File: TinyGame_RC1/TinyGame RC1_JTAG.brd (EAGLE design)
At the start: 38 x 22 mm, 41 parts, among them J1 AUDIO-CONNECTOR-6P-SMD-344003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, K1 BUTTON-4P-3100010P1, K2 BUTTON-4P-3100010P1, K3 BUTTON-4P-3100010P1, K4 BUTTON-4P-3100010P1, U1 MKL02Z32VFK4

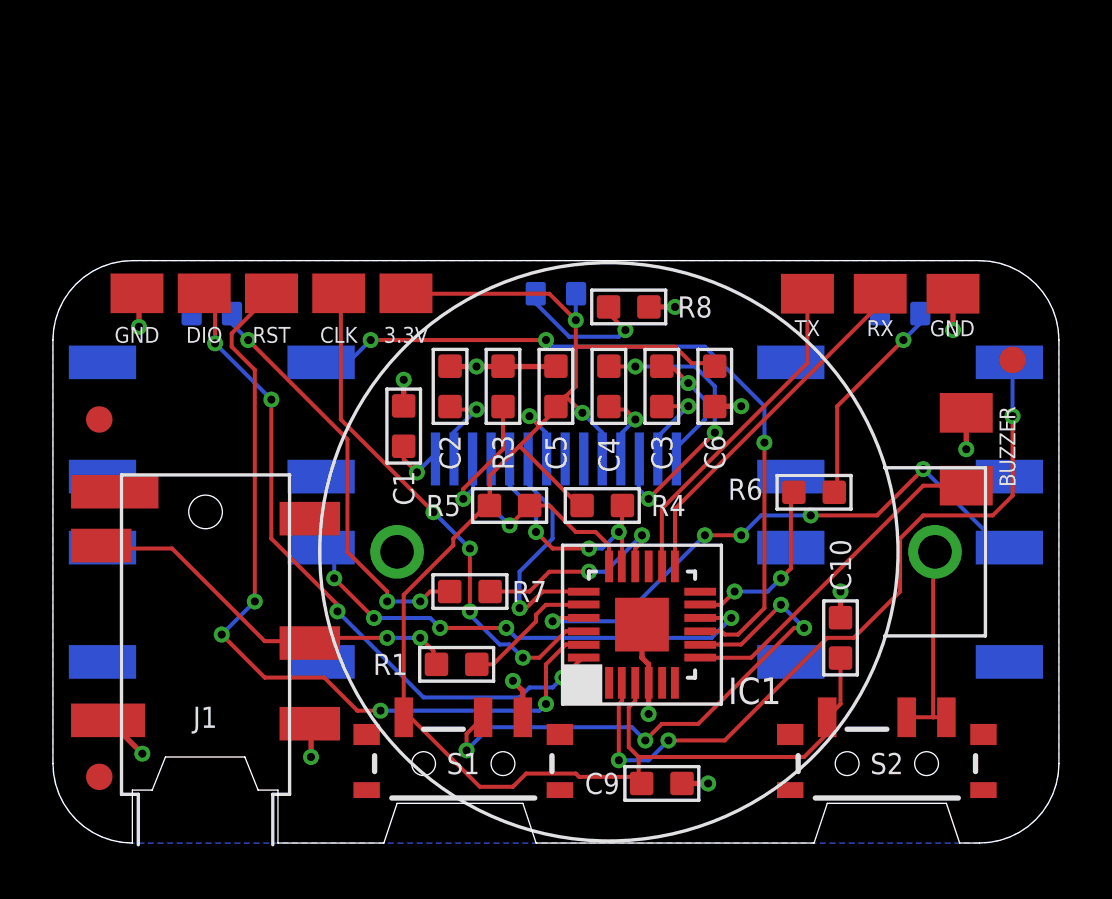
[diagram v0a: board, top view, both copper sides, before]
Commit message: Moved some stuff around - added testjig and jtag adapter
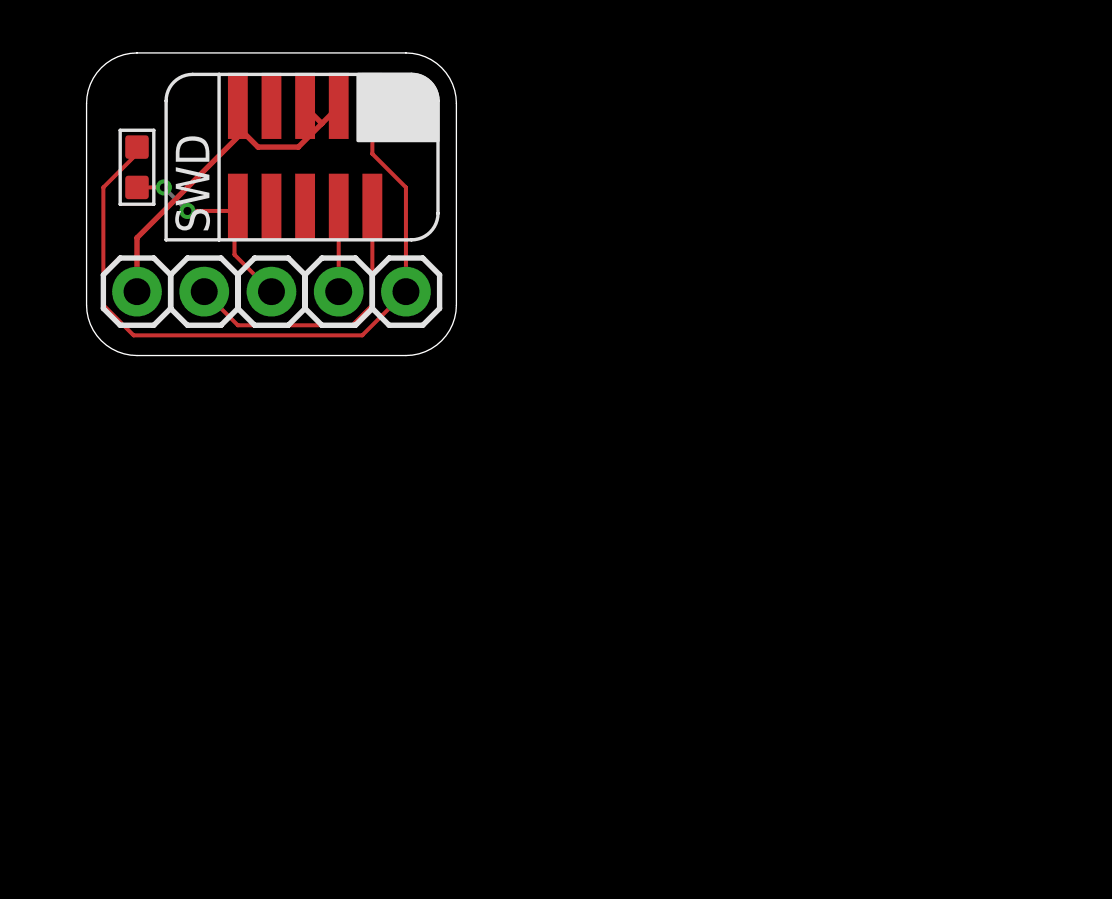
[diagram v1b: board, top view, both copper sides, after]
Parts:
- removed AUDIOGND, AUDIOSIG, PTA6_MISO1, PTA6_MISO2, PTA6_MISO3, PTA6_MISO4, PTA6_MISO5, PTB1_RXTX, PTB2_TXRX, PTB2_TXRX2: M01SMD-4.5X1.5, SparkFun-Connectors:PAD-1.5X4.5
- removed BATTERY_1: BATTERY_1236_C, MicroGameboyParts:BATTERY_1236_C
- removed C1: 2.2uF, OPL:C0603
- removed C10: 100nF, OPL:C0603
- removed C2: 4.7uF, OPL:C0603
- removed C3, C4, C5, C6, C9: 1uF, OPL:C0603
- removed D1, D2, D3: YELLOW, OPL:LED0603
- removed J1: AUDIO-CONNECTOR-6P-SMD-3440030P1, OPL:6P-SMD-3.5
- removed K1, K2, K3, K4: BUTTON-4P-3100010P1, zephod-components:4P-SMD-6.0X6.0X5.0H
- removed R1, R4, R5, R6, R7: 2K, OPL:R0603
- removed R3: 390K, OPL:R0603
- removed S1, S2: (no value), SparkFun-Electromechanical:SWITCH-SPST-SMD-A
- removed U$1: 0.49"OLEDFOLDED, zephod-tft:0.49"-FPC-0.7-14-FOLDED
- removed U$2, U$3, U$4: FIDUCIAL, adafruit:FIDUCIAL_1MM
- removed U1: MKL02Z32VFK4, FarnellThings:QFN50P400X400X100-25N
- added 3.3V_1, GND_2, RESET, SWCLK, SWDIO: M01PTH, SparkFun-Connectors:1X01
- added SWD1: CORTEX_SWDVERT, carrilib with jtags:SWD_VERTICAL
- R8: value 2K -> 10K
- moved R8 19.3 mm to (3.17, 25.5), turned to 90 degrees
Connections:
- removed net AUDIO: AUDIOSIG.P$1, U1.7
- removed net AUDIOSELECTOR: S1.2, U1.8
- removed net BUTTON1: K1.1, U1.2
- removed net BUTTON2: K3.1, U1.9
- removed net BUTTON3: K4.1, U1.10
- removed net BUTTON4: K2.1, U1.21
- removed net DATAIN: R1.2, U1.20
- removed net LED1: R6.2, U1.11
- removed net LED2: R7.2, U1.16
- removed net N$10: C1.1, U$1.P$14
- removed net N$11: C2.2, U$1.P$13
- removed net N$12: C3.1, U$1.P$2
- removed net N$13: C4.1, U$1.P$4
- removed net N$14: D2.+, R7.1
- removed net N$19: D3.-, R8.2
- removed net N$2: J1.L, J1.R, R1.1
- removed net N$20: BATTERY_1.+, S2.1, S2.2
- removed net N$3: C3.2, U$1.P$1
- removed net N$4: C4.2, U$1.P$3
- removed net N$6: D1.+, R6.1
- removed net N$9: R3.2, U$1.P$12
- removed net OLED_RESET: U$1.P$9, U1.19
- removed net OLED_SCL: R4.1, U$1.P$10, U1.17
- removed net OLED_SDA: R5.1, U$1.P$11, U1.18
- removed net PTB1: PTB1_RXTX.P$1, U1.13
- removed net PTB2: PTB2_TXRX.P$1, U1.14
- net 3.3V: now also 3.3V_1.1, R8.2, SWD1.1; no longer C10.2, C5.2, C6.2, C9.2, D3.+, PTA6_MISO1.P$1, R4.2, R5.2, S1.3, S2.3, U$1.P$5, U$1.P$8, U1.3
- net GND: now also GND_2.1, SWD1.3, SWD1.5, SWD1.9; no longer AUDIOGND.P$1, BATTERY_1.-, C1.2, C10.1, C2.1, C5.1, C6.1, C9.1, D1.-, D2.-, J1.COM1, J1.COM2, K1.2, K1.3, K2.2, K2.3, K3.2, K3.3, K4.2, K4.3, PTA6_MISO5.P$1, PTB2_TXRX2.P$1, R3.1, R8.1, S1.1, U$1.P$7, U1.25, U1.4
- net RESET: now also R8.1, RESET.1, SWD1.10; no longer PTA6_MISO4.P$1, U1.23
- net SWCLK: now also SWCLK.1, SWD1.4; no longer PTA6_MISO3.P$1, U1.22
- net SWDIO: now also SWD1.2, SWDIO.1; no longer PTA6_MISO2.P$1, U1.24
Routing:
- net 3.3V: track 65.7 -> 26.6 mm, vias 3 -> 0
- net BUTTON2: track 28.6 -> 0.00 mm, vias 3 -> 0
- net BUTTON1: track 28.3 -> 0.00 mm, vias 3 -> 0
- net RESET: track 31.2 -> 8.09 mm, vias 4 -> 2
- net BUTTON4: track 22.1 -> 0.00 mm, vias 5 -> 0
- net AUDIOSELECTOR: track 21.5 -> 0.00 mm, vias 4 -> 0
- net BUTTON3: track 18.8 -> 0.00 mm, vias 5 -> 0
- net SWCLK: track 19.6 -> 3.21 mm, vias 4 -> 0
- net N$14: track 15.8 -> 0.00 mm, vias 3 -> 0
- net N$2: track 15.0 -> 0.00 mm, vias 2 -> 0
- net SWDIO: track 25.4 -> 10.9 mm, vias 4 -> 0
- net PTB1: track 13.5 -> 0.00 mm
- net AUDIO: track 12.7 -> 0.00 mm
- net PTB2: track 12.6 -> 0.00 mm
- net N$4: track 11.3 -> 0.00 mm, vias 3 -> 0
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- removed copper zone on layer 16, net GND
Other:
- board size 38 x 22 mm -> 14 x 11.4 mm
- board text removed: "BUZZER"
- board text removed: "CLK"
- board text removed: "DIO"
- board text removed: "IC1"
- board text removed: "RST"
- board text removed: "RX"
- board text removed: "TX"
- board text removed: "TinyGame"
